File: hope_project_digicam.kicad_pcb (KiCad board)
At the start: 2 copper layers, 46 parts, among them J1 USB_C_Receptacle_USB2.0_16P, J2 SD_Card_Port, J3 Camera_Pin_Out, J4 Lipo batt in, J5 TFT_Pin_Socket, J6 extra, Q1 NMOS, Q2 PMOS, SW1 Cam Trigger, SW2 Reset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

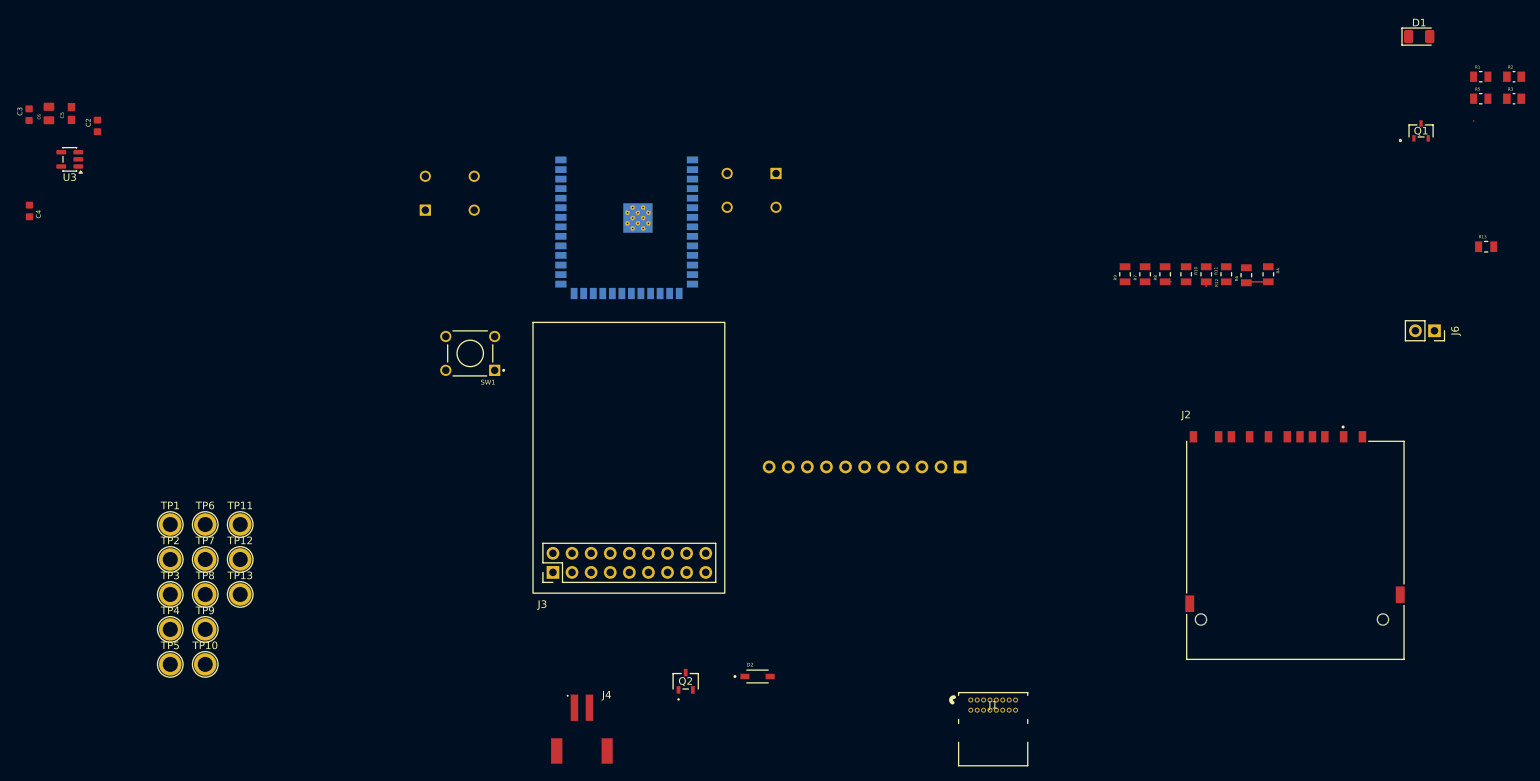
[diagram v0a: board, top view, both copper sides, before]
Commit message: fixed footprints, laid stuff out, didn't route yet :(
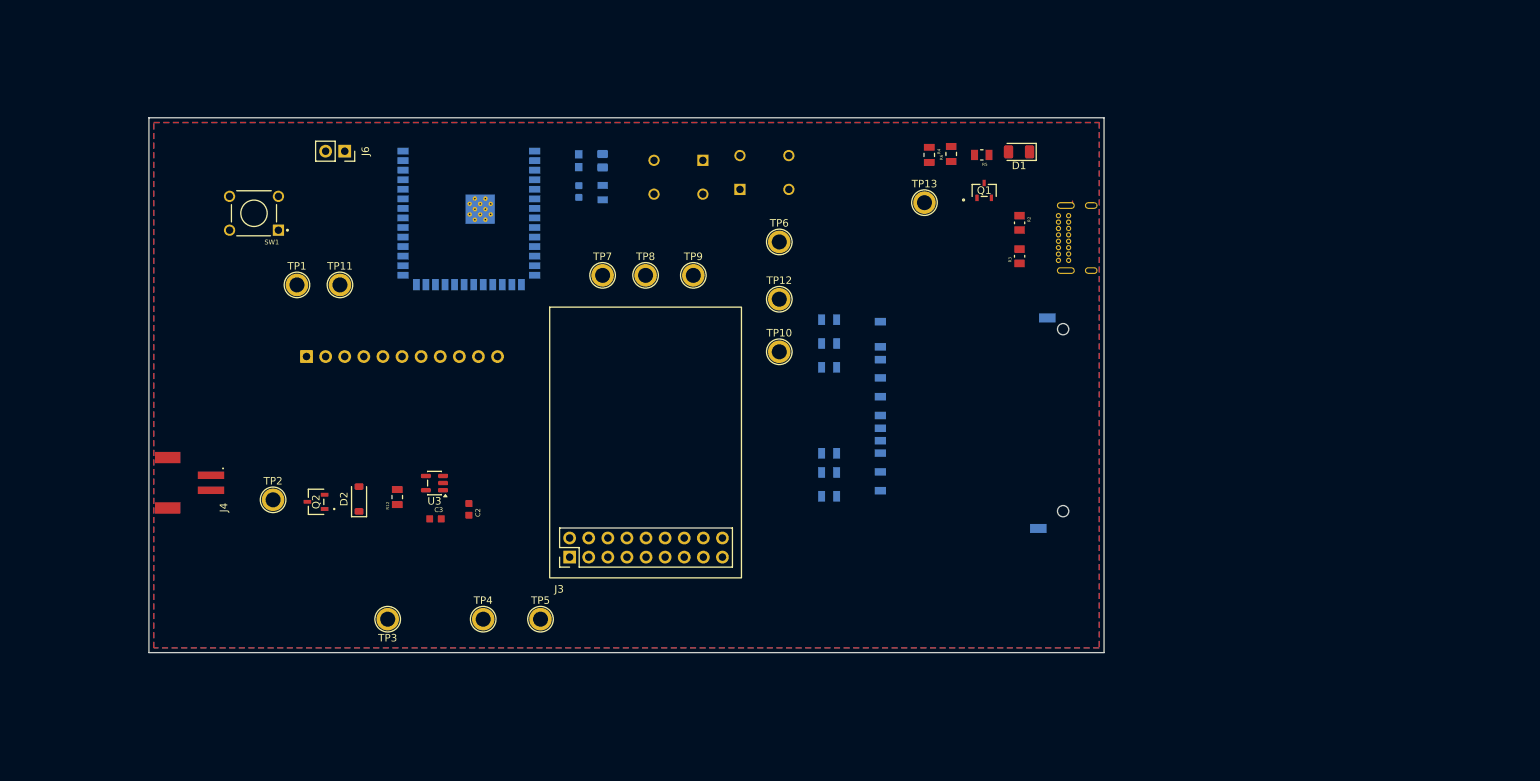
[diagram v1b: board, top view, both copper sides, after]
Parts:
- C4, C5, C6, J2, R1, R10, R11, R13, R7, R8, R9: moved to B.Cu
- D2: footprint HOPE DigiCam:Shottky_Diode -> Diode_SMD:D_SOD-123
- J1: footprint HOPE DigiCam:USB_C_Receptacle -> Connector_USB:USB_C_Receptacle_GCT_USB4085; moved to B.Cu
- moved J6 146.9 mm to (104.8, 57.1)
- moved R1 117.8 mm to (139.1, 62.6), turned to 90 degrees
- moved R12 114.1 mm to (111.8, 103.1)
- moved TP13 104.8 mm to (181.9, 64.0)
- moved R13 87.9 mm to (169.2, 79.5)
- moved TP10 86.9 mm to (162.6, 83.8)
- moved TP6 85.1 mm to (162.6, 69.2)
- moved TP9 80.2 mm to (151.1, 73.7)
- moved TP12 79.6 mm to (162.6, 76.8)
- moved C3 76.2 mm to (116.8, 106.0), turned to 0 degrees
- moved C6 73.9 mm to (139.1, 58.4)
- moved C4 73.1 mm to (135.9, 62.5), turned to 90 degrees
- moved TP8 72.3 mm to (144.8, 73.7)
- moved C2 71.0 mm to (121.3, 104.8), turned to -90 degrees
- moved R3 69.0 mm to (194.5, 71.1), turned to 90 degrees
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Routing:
- net Net-(Q1-G): track 2.97 -> 0.00 mm
- net +3.3V: track 0.94 -> 0.00 mm
- net /SD_DAT2: track 0.65 -> 0.00 mm
- net /PWR_IN: track 0.53 -> 0.00 mm
- added copper zone on F.Cu, net +3.3V
- added copper zone on B.Cu, net GND
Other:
- board outline added: 127 x 71.1 mm
